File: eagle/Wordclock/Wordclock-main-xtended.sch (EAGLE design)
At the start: 66 parts, among them IC1 MEGA8-P, J1 AVR_SPI_PRG_6PTH, Q1 16MHz, T1 EBC pinout

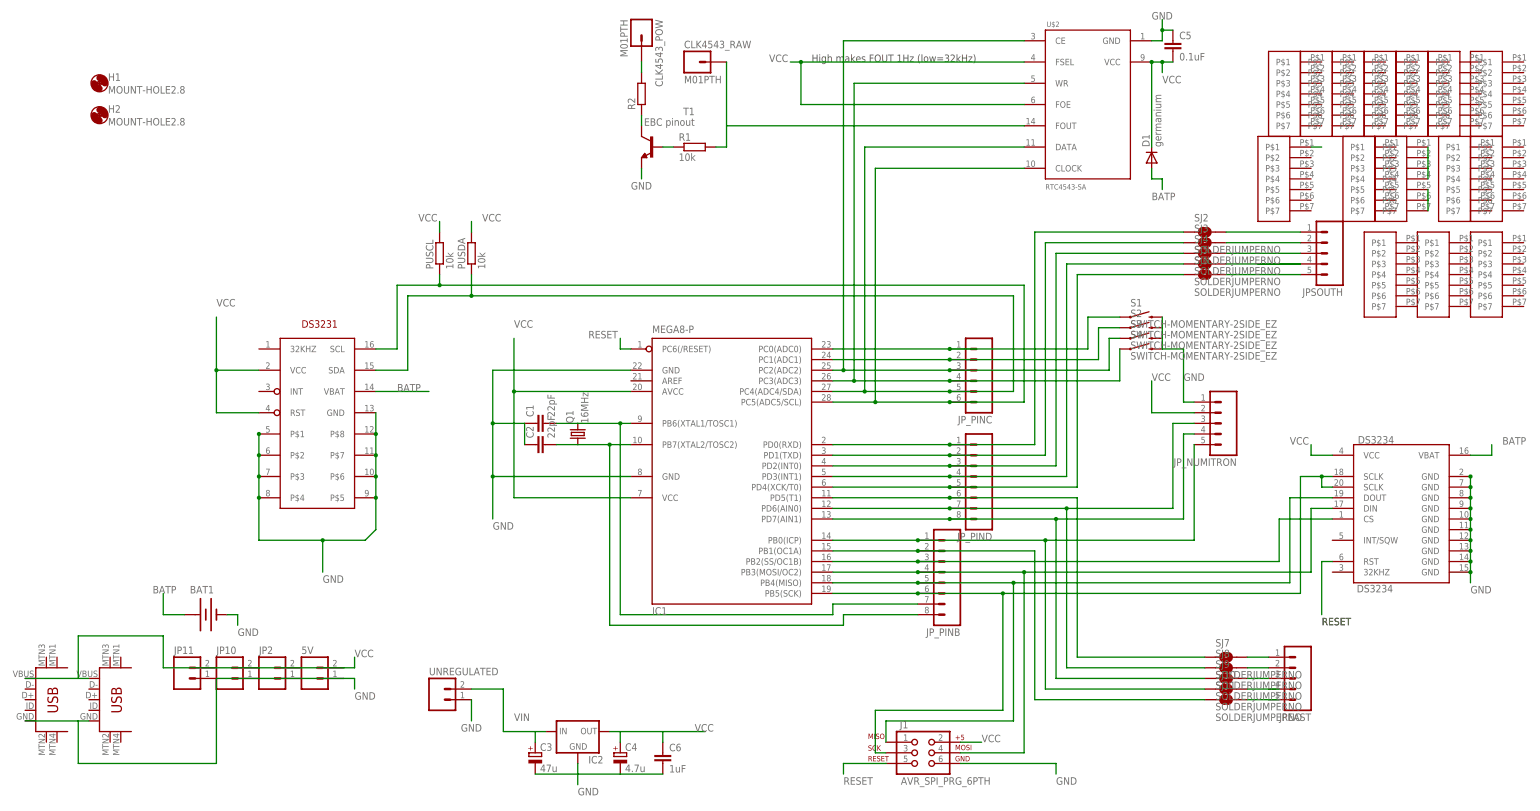
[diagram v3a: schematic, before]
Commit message: Extended wordlock main board sent to production.
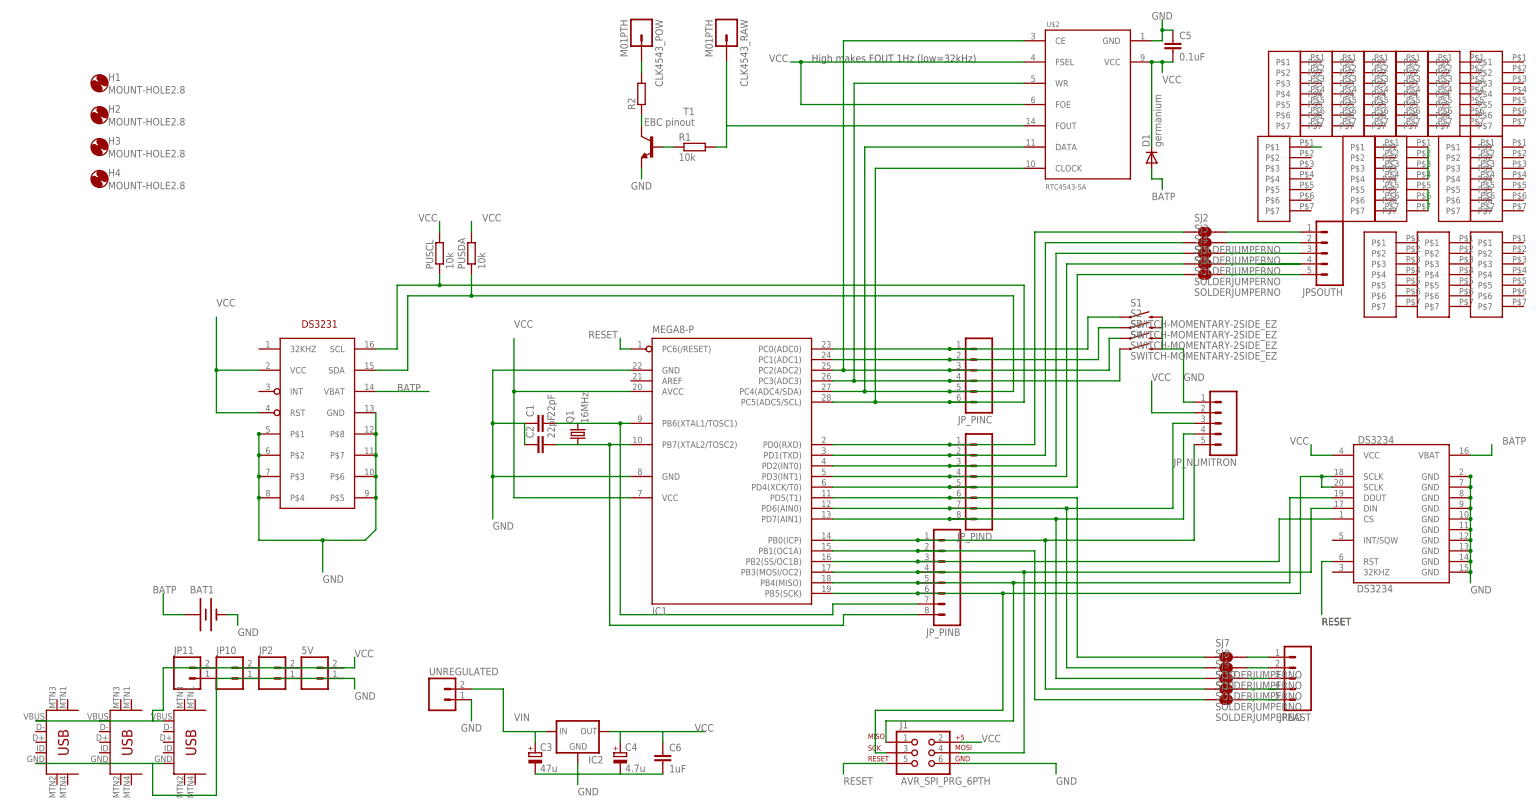
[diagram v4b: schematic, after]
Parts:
- added H3, H4: MOUNT-HOLE2.8, holes:MOUNT-HOLE2.8
- added U$7: USB-MINIB-5PIN, SparkFun-Connectors:USB-MINIB-5PIN
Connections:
- net GND: now also U$7.GND
- net VCC: now also U$7.VBUS
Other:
- moved on the sheet: CLK4543_RAW
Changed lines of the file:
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@@
 <part name="H1" library="holes" deviceset="MOUNT-HOLE" device="2.8"/>
 <part name="H2" library="holes" deviceset="MOUNT-HOLE" device="2.8"/>
+<part name="H3" library="holes" deviceset="MOUNT-HOLE" device="2.8"/>
+<part name="U$7" library="SparkFun-Connectors" deviceset="USB-MINIB" device="-5PIN"/>
+<part name="H4" library="holes" deviceset="MOUNT-HOLE" device="2.8"/>
 </parts>
 <sheets>
@@
 <instance part="D1" gate="G$1" x="160.02" y="129.54" rot="R90"/>
 <instance part="C5" gate="G$1" x="165.1" y="157.48"/>
-<instance part="CLK4543_RAW" gate="G$1" x="50.8" y="152.4"/>
+<instance part="CLK4543_RAW" gate="G$1" x="58.42" y="160.02" rot="R270"/>
 <instance part="T1" gate="G$1" x="40.64" y="132.08" rot="MR0"/>
 <instance part="R1" gate="G$1" x="50.8" y="132.08"/>
@@
 <instance part="JP10" gate="G$1" x="-60.96" y="5.08"/>
 <instance part="JP11" gate="G$1" x="-71.12" y="5.08"/>
-<instance part="U$11" gate="G$1" x="-91.44" y="-5.08"/>
-<instance part="U$12" gate="G$1" x="-106.68" y="-5.08"/>
+<instance part="U$11" gate="G$1" x="-73.66" y="-15.24"/>
+<instance part="U$12" gate="G$1" x="-88.9" y="-15.24"/>
 <instance part="H1" gate="G$1" x="-91.44" y="147.32"/>
 <instance part="H2" gate="G$1" x="-91.44" y="139.7"/>
+<instance part="H3" gate="G$1" x="-91.44" y="132.08"/>
+<instance part="U$7" gate="G$1" x="-104.14" y="-15.24"/>
+<instance part="H4" gate="G$1" x="-91.44" y="124.46"/>
 </instances>
 <busses>
@@
 <wire x1="-63.5" y1="5.08" x2="-53.34" y2="5.08" width="0.1524" layer="91"/>
 <pinref part="U$11" gate="G$1" pin="GND"/>
-<wire x1="-93.98" y1="-5.08" x2="-96.52" y2="-5.08" width="0.1524" layer="91"/>
-<wire x1="-96.52" y1="-5.08" x2="-96.52" y2="-15.24" width="0.1524" layer="91"/>
-<wire x1="-96.52" y1="-15.24" x2="-63.5" y2="-15.24" width="0.1524" layer="91"/>
-<wire x1="-63.5" y1="-15.24" x2="-63.5" y2="5.08" width="0.1524" layer="91"/>
+<wire x1="-76.2" y1="-15.24" x2="-78.74" y2="-15.24" width="0.1524" layer="91"/>
+<wire x1="-78.74" y1="-15.24" x2="-78.74" y2="-22.86" width="0.1524" layer="91"/>
+<wire x1="-78.74" y1="-22.86" x2="-63.5" y2="-22.86" width="0.1524" layer="91"/>
+<wire x1="-63.5" y1="-22.86" x2="-63.5" y2="5.08" width="0.1524" layer="91"/>
 <pinref part="U$12" gate="G$1" pin="GND"/>
-<wire x1="-109.22" y1="-5.08" x2="-96.52" y2="-5.08" width="0.1524" layer="91"/>
+<wire x1="-91.44" y1="-15.24" x2="-78.74" y2="-15.24" width="0.1524" layer="91"/>
+<pinref part="U$7" gate="G$1" pin="GND"/>
+<wire x1="-91.44" y1="-15.24" x2="-106.68" y2="-15.24" width="0.1524" layer="91"/>
 </segment>
 <segment>
@@
 <wire x1="-63.5" y1="7.62" x2="-53.34" y2="7.62" width="0.1524" layer="91"/>
 <pinref part="U$11" gate="G$1" pin="VBUS"/>
-<wire x1="-93.98" y1="5.08" x2="-96.52" y2="5.08" width="0.1524" layer="91"/>
-<wire x1="-96.52" y1="5.08" x2="-96.52" y2="15.24" width="0.1524" layer="91"/>
-<wire x1="-96.52" y1="15.24" x2="-76.2" y2="15.24" width="0.1524" layer="91"/>
-<wire x1="-76.2" y1="15.24" x2="-76.2" y2="7.62" width="0.1524" layer="91"/>
+<wire x1="-76.2" y1="-5.08" x2="-78.74" y2="-5.08" width="0.1524" layer="91"/>
+<wire x1="-78.74" y1="-5.08" x2="-78.74" y2="-2.54" width="0.1524" layer="91"/>
+<wire x1="-78.74" y1="-2.54" x2="-76.2" y2="-2.54" width="0.1524" layer="91"/>
+<wire x1="-76.2" y1="-2.54" x2="-76.2" y2="7.62" width="0.1524" layer="91"/>
 <wire x1="-76.2" y1="7.62" x2="-63.5" y2="7.62" width="0.1524" layer="91"/>
 <pinref part="U$12" gate="G$1" pin="VBUS"/>
-<wire x1="-109.22" y1="5.08" x2="-96.52" y2="5.08" width="0.1524" layer="91"/>
-</segment>
-<segment>
+<wire x1="-91.44" y1="-5.08" x2="-78.74" y2="-5.08" width="0.1524" layer="91"/>
+<pinref part="U$7" gate="G$1" pin="VBUS"/>
+<wire x1="-91.44" y1="-5.08" x2="-106.68" y2="-5.08" width="0.1524" layer="91"/>
+</segment>
+<segment>
